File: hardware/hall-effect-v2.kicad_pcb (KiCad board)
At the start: 2 copper layers, 15 x 25 mm, 24 parts, among them P1 CON-SENSOR2, P2 DEBUG, P3 BOOT, U1 XMC1XXX24, U2 DRV023, U3 DRILL, U4 DRILL, U5 DRILL, U6 DRILL

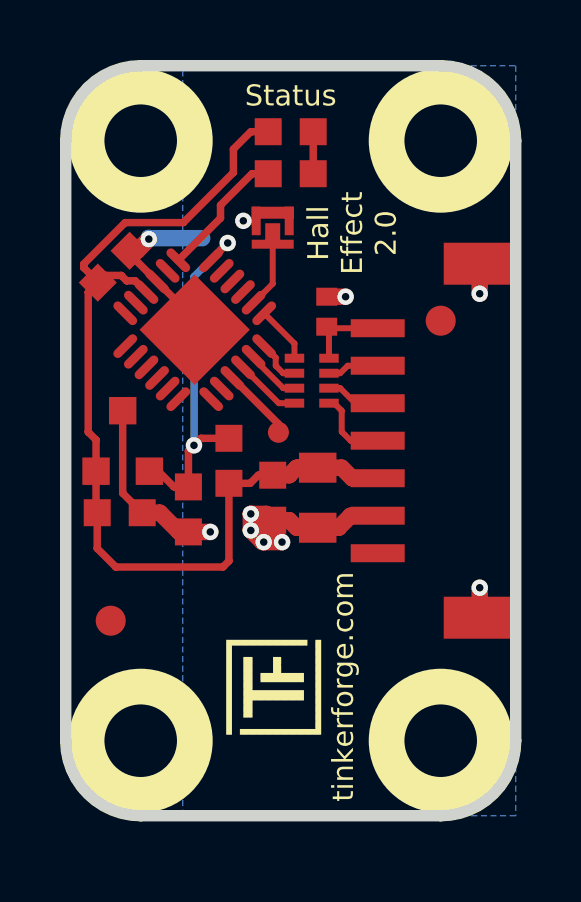
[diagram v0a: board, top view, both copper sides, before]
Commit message: Change input pin to P0.0
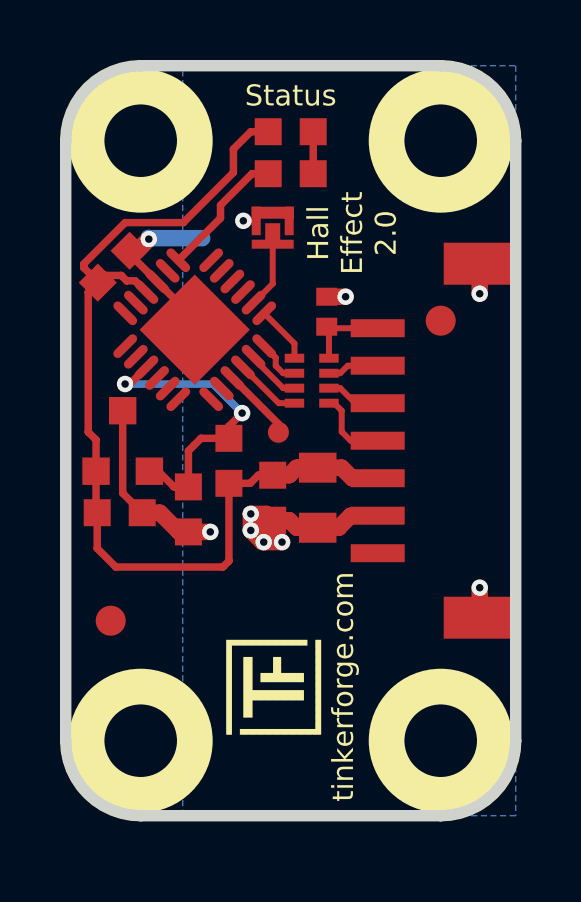
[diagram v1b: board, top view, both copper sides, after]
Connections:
- U1 pad 15: Net-(U1-Pad15) -> OUT
- U1 pad 6: OUT -> Net-(U1-Pad6)
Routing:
- net OUT: track 12.7 -> 11.0 mm
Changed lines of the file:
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@@
     (thickness 1.6002)
     (drawings 12)
-    (tracks 151)
+    (tracks 154)
     (zones 0)
     (modules 24)
@@
   (title_block
     (title "Hall Effect Bricklet")
-    (date 2018-06-27)
+    (date 2018-07-06)
     (rev 2.0)
     (company "Tinkerforge GmbH")
@@
   )
   (setup
-    (last_trace_width 0.55)
+    (last_trace_width 0.25)
     (user_trace_width 0.2)
     (user_trace_width 0.25)
@@
   (net 23 "Net-(U1-Pad13)")
   (net 24 "Net-(U1-Pad14)")
-  (net 25 "Net-(U1-Pad15)")
-  (net 26 "Net-(U1-Pad16)")
-  (net 27 "Net-(U1-Pad17)")
-  (net 28 "Net-(U1-Pad18)")
-  (net 29 "Net-(U1-Pad19)")
-  (net 30 "Net-(U1-Pad20)")
+  (net 25 "Net-(U1-Pad16)")
+  (net 26 "Net-(U1-Pad17)")
+  (net 27 "Net-(U1-Pad18)")
+  (net 28 "Net-(U1-Pad19)")
+  (net 29 "Net-(U1-Pad20)")
+  (net 30 "Net-(U1-Pad6)")
   (net_class Default "Dies ist die voreingestellte Netzklasse."
     (clearance 0.15)
@@
     (add_net "Net-(U1-Pad13)")
     (add_net "Net-(U1-Pad14)")
-    (add_net "Net-(U1-Pad15)")
     (add_net "Net-(U1-Pad16)")
     (add_net "Net-(U1-Pad17)")
@@
     (add_net "Net-(U1-Pad4)")
     (add_net "Net-(U1-Pad5)")
+    (add_net "Net-(U1-Pad6)")
     (add_net "Net-(U1-Pad8)")
     (add_net OUT)
@@
       (net 19 "Net-(U1-Pad5)"))
     (pad 6 smd oval (at -2.025 1.25 225) (size 1 0.3) (layers Vorderseite F.Paste F.Mask)
-      (net 8 OUT))
+      (net 30 "Net-(U1-Pad6)"))
     (pad 7 smd oval (at -1.25 2.025 315) (size 1 0.3) (layers Vorderseite F.Paste F.Mask)
       (net 12 "Net-(R3-Pad1)"))
@@
       (net 24 "Net-(U1-Pad14)"))
     (pad 15 smd oval (at 2.025 0.25 225) (size 1 0.3) (layers Vorderseite F.Paste F.Mask)
-      (net 25 "Net-(U1-Pad15)"))
+      (net 8 OUT))
     (pad 16 smd oval (at 2.025 -0.25 225) (size 1 0.3) (layers Vorderseite F.Paste F.Mask)
-      (net 26 "Net-(U1-Pad16)"))
+      (net 25 "Net-(U1-Pad16)"))
     (pad 17 smd oval (at 2.025 -0.75 225) (size 1 0.3) (layers Vorderseite F.Paste F.Mask)
-      (net 27 "Net-(U1-Pad17)"))
+      (net 26 "Net-(U1-Pad17)"))
     (pad 18 smd oval (at 2.025 -1.25 225) (size 1 0.3) (layers Vorderseite F.Paste F.Mask)
-      (net 28 "Net-(U1-Pad18)"))
+      (net 27 "Net-(U1-Pad18)"))
     (pad 19 smd oval (at 1.25 -2.025 315) (size 1 0.3) (layers Vorderseite F.Paste F.Mask)
-      (net 29 "Net-(U1-Pad19)"))
+      (net 28 "Net-(U1-Pad19)"))
     (pad 20 smd oval (at 0.75 -2.025 315) (size 1 0.3) (layers Vorderseite F.Paste F.Mask)
-      (net 30 "Net-(U1-Pad20)"))
+      (net 29 "Net-(U1-Pad20)"))
     (pad 21 smd oval (at 0.25 -2.025 315) (size 1 0.3) (layers Vorderseite F.Paste F.Mask)
       (net 10 "Net-(P2-Pad1)"))
@@
   (segment (start 53.3 38.55) (end 51.65 38.55) (width 0.2) (layer Vorderseite) (net 7))
   (segment (start 51.65 38.55) (end 51.675 38.575) (width 0.2) (layer Vorderseite) (net 7))
-  (via (at 47.175 42.455) (size 0.55) (drill 0.25) (layers Vorderseite Rückseite) (net 8))
-  (segment (start 47.748008 36.261992) (end 48.3 35.71) (width 0.25) (layer Vorderseite) (net 8))
-  (via (at 48.3 35.71) (size 0.55) (drill 0.25) (layers Vorderseite Rückseite) (net 8))
-  (segment (start 47.18 36.83) (end 48.3 35.71) (width 0.25) (layer Rückseite) (net 8))
-  (segment (start 47.18 42.46) (end 47.18 36.83) (width 0.25) (layer Rückseite) (net 8))
-  (segment (start 47.18 42.46) (end 47.175 42.455) (width 0.25) (layer Rückseite) (net 8))
-  (segment (start 47.748008 36.261992) (end 47.748008 36.284225) (width 0.25) (layer Vorderseite) (net 8))
+  (segment (start 48.34 42.22) (end 48.34 41.82) (width 0.25) (layer Vorderseite) (net 8))
+  (segment (start 48.34 41.82) (end 48.78 41.38) (width 0.25) (layer Vorderseite) (net 8))
+  (segment (start 45.046447 40.4) (end 45.591332 39.855115) (width 0.25) (layer Vorderseite) (net 8))
+  (segment (start 44.89 40.4) (end 45.046447 40.4) (width 0.25) (layer Vorderseite) (net 8))
+  (segment (start 44.88 40.41) (end 44.89 40.4) (width 0.25) (layer Vorderseite) (net 8))
+  (via (at 44.88 40.41) (size 0.55) (drill 0.25) (layers Vorderseite Rückseite) (net 8))
+  (segment (start 47.81 40.41) (end 44.88 40.41) (width 0.25) (layer Rückseite) (net 8))
+  (segment (start 48.78 41.38) (end 47.81 40.41) (width 0.25) (layer Rückseite) (net 8))
+  (via (at 48.78 41.38) (size 0.55) (drill 0.25) (layers Vorderseite Rückseite) (net 8))
   (segment (start 46.99 43.84) (end 46.99 42.64) (width 0.25) (layer Vorderseite) (net 8))
   (segment (start 46.99 42.64) (end 47.175 42.455) (width 0.25) (layer Vorderseite) (net 8))
@@
   (segment (start 50.525 41.0493) (end 50.002853 41.0493) (width 0.2) (layer Vorderseite) (net 16))
   (segment (start 50.002853 41.0493) (end 48.808668 39.855115) (width 0.2) (layer Vorderseite) (net 16))
+  (segment (start 47.748008 36.261992) (end 47.748008 36.284225) (width 0.25) (layer Vorderseite) (net 30))
   (zone (net 1) (net_name GND) (layer Rückseite) (hatch edge 0.508)
     (connect_pads (clearance 0.24892))
